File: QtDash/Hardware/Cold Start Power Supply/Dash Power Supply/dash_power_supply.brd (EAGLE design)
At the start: 160 x 100 mm, 26 parts, among them IC1 LM5060, Q1 IPB042N10N3GATMA1, Q2 IPB042N10N3GATMA1, Q3 600mA/40V

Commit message: bugfix/hardware-revA-issues: 	- added lm3488 5V SEPIC DC/DC converter -- components selected and first draft of layout 	- TODO: select components for input protection and layout the input proectection 	- TODO: add second 5V DC/DC
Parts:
- added C10, C11: 100u, dash_power_supply:C1210
- added C12: 4.7u, digital_dash:0603
- added C13: .68u, digital_dash:0603
- added C14, C15: 1n, digital_dash:0603
- added C6: 100n, digital_dash:0603
- added C7, C8, C9: 3.3u, dash_power_supply:PANASONIC_C
- added D10, D11: 3A/10V/280mV, SparkFun-DiscreteSemi:SOD-323
- added D9: STPS8H100G-TR, dash_power_supply:TO263
- added IC2: LM3488, dash_power_supply:VSSOP-8
- added L1: DRQ127-4R7-R, dash_power_supply:DRQ127
- added Q4: BSC027N04LSG, dash_power_supply:TDSON
- added R10: 20k, SparkFun-Resistors:0603
- added R11: 100R, digital_dash:0603
- added R12: 30.9k 1%, dash_power_supply:R1206
- added R13: 10k 1%, digital_dash:0603
- added R14: 75k, SparkFun-Resistors:0603
- added R15: 6mOhm, dash_power_supply:3216
- added R16: 270 1%, digital_dash:0603
- added R17: 0, SparkFun-Resistors:0603
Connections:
- removed net VOUT: D2.C, D3.C, Q2.3, R9.2
- new net 5V: C10.1, C11.1, D11.A, D9.3, R12.2
- new net N$11: Q4.4, R17.2
- new net N$12: C6.1, IC2.8, R10.1
- new net N$13: IC2.3, R12.1, R13.2
- new net N$15: IC2.6, R17.1
- new net N$16: C15.1, IC2.1, R11.1
- new net N$17: Q4.1, Q4.2, Q4.3, R11.2, R15.2
- new net N$18: C12.1, L1.3, Q4.5
- new net N$19: C12.2, D9.2, L1.4
- new net N$20: C14.1, IC2.2, R16.2
- new net N$21: C13.1, R16.1
- new net N$22: IC2.7, R14.2
- new net N$23: D10.C, R5.1
- new net VBATT: C7.+, C8.+, C9.+, D2.C, D3.C, L1.1, Q2.3, R10.2, R9.2
- net GND: now also C10.2, C11.2, C13.2, C14.2, C15.2, C6.2, C7.-, C8.-, C9.-, IC2.4, IC2.5, L1.2, R13.1, R14.1, R15.1
- net VIN_LM5060: now also D10.A, D11.C; no longer R5.1
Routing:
- net VBATT: track 0.00 -> 45.4 mm, vias 0 -> 2
- net N$17: track 0.00 -> 29.2 mm, vias 0 -> 2
- net N$13: track 0.00 -> 11.1 mm
- net N$16: track 0.00 -> 8.13 mm
- net N$12: track 0.00 -> 7.01 mm
- net N$20: track 0.00 -> 6.23 mm
- net N$22: track 0.00 -> 3.69 mm
- net N$15: track 0.00 -> 3.69 mm
- net N$11: track 0.00 -> 3.56 mm
- net N$21: track 0.00 -> 3.24 mm
- added copper zone on layer 1, net 5V
- added copper zone on layer 1, net GND
- added copper zone on layer 1, net N$14
- added copper zone on layer 1, net N$17
- added copper zone on layer 1, net N$18
- added copper zone on layer 1, net N$19
- added copper zone on layer 1, net VBATT

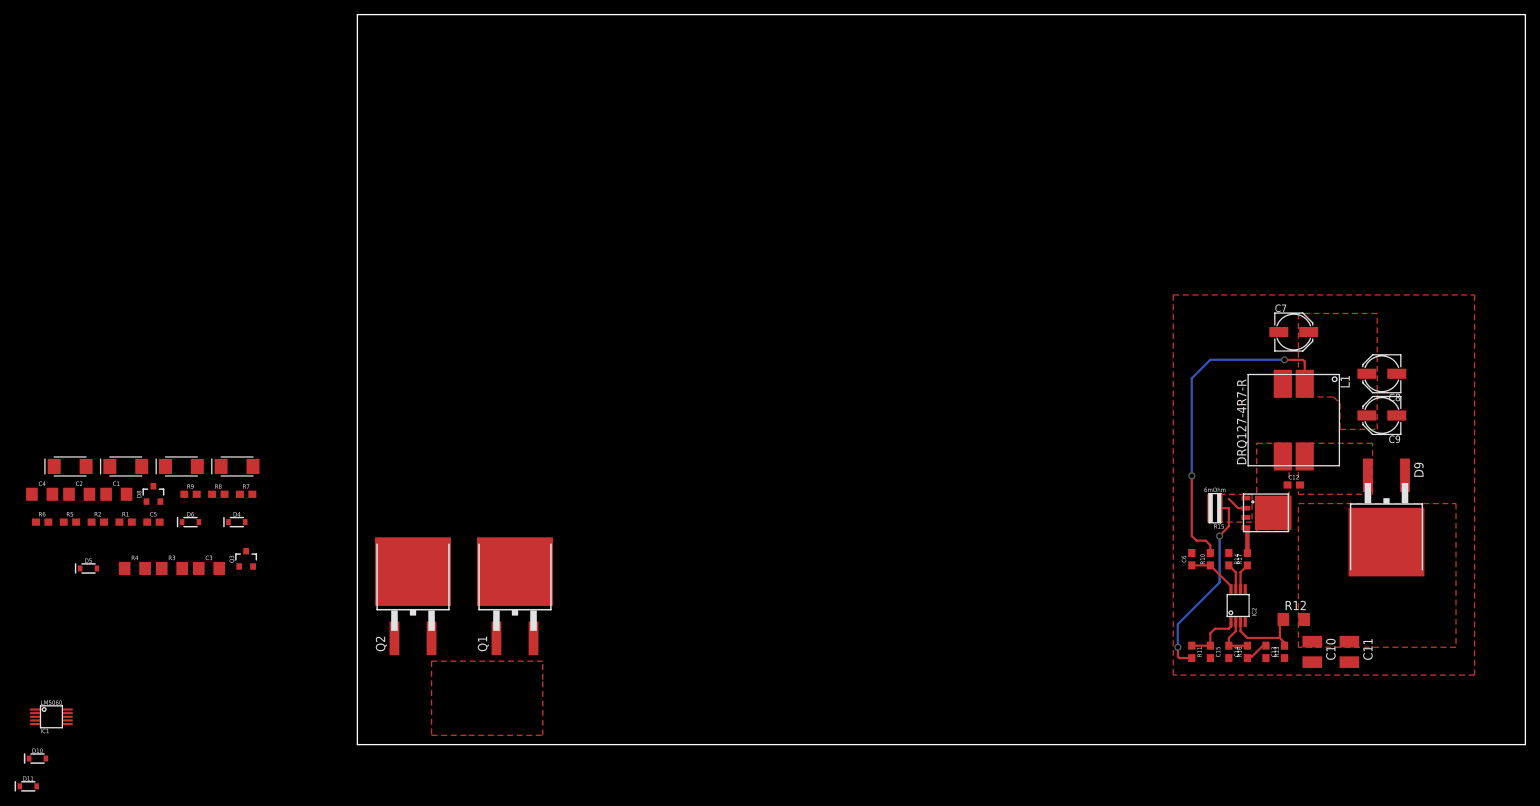
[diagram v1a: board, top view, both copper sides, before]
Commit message: bugfix/hardware-revA-issues: 	- first draft of cold start power supply board layout -- passed DRC
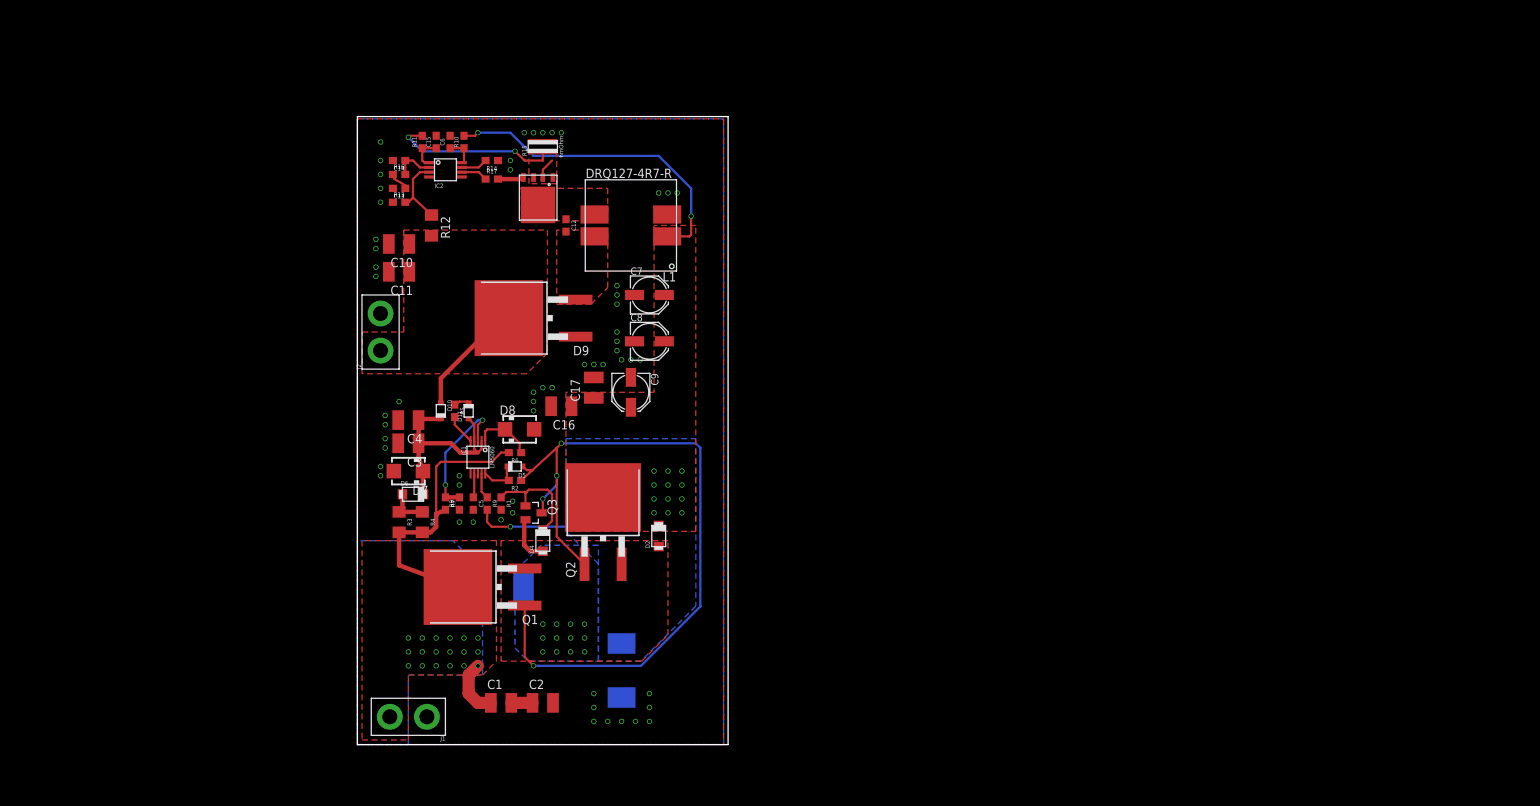
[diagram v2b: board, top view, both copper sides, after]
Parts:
- added C16: 4.7u, dash_power_supply:C1210
- added C17: 0.1u, dash_power_supply:C1210
- added J1, J2: (no value), SparkFun-Connectors:1X02_XTRA_BIG
- C1, C2, C4: value (none) -> 0.1u; device SparkFun-Capacitors:1206 -> dash_power_supply:C1210
- C3: value 4.7uF -> 4.7u; device SparkFun-Capacitors:1206 -> dash_power_supply:C1210
- C5: value 0.1uF -> 100n; device SparkFun-Capacitors:0603 -> digital_dash:0603
- D1, D3: device SparkFun-DiscreteSemi:DO-214AC -> dash_power_supply:SMC
- D10, D11, D5: value 3A/10V/280mV -> NSR0170HT1G; device SparkFun-DiscreteSemi:SOD-323 -> dash_power_supply:SOD-323
- D2: device SparkFun-DiscreteSemi:DO-214AC -> dash_power_supply:D0-219AB
- D4, D6: value 250mA/100V -> 200V; device SparkFun-DiscreteSemi:SOD-323 -> dash_power_supply:D0-219AB
- D7: value SMAJ36A -> 24V; device SparkFun-DiscreteSemi:DO-214AC -> dash_power_supply:SMA
- D8: value 68V -> 24V; device SparkFun-DiscreteSemi:SOT23-3 -> dash_power_supply:SMA
- Q3: value 600mA/40V -> BC816-25HVL; device SparkFun-DiscreteSemi:SOT23-3 -> dash_power_supply:SOT23
- moved C11 140.2 mm to (5.71, 64.8), turned to 180 degrees
- moved C10 137.0 mm to (5.71, 68.6), turned to 180 degrees
- moved R13 136.0 mm to (5.71, 74.3), turned to 0 degrees
- moved C13 134.7 mm to (5.71, 76.2), turned to 180 degrees
- moved R16 133.3 mm to (5.71, 78.1), turned to 0 degrees
- moved C14 132.1 mm to (5.71, 80.0), turned to 180 degrees
- moved R12 129.9 mm to (10.2, 71.1), turned to 270 degrees
- moved C15 127.0 mm to (10.8, 82.5), turned to 90 degrees
- moved R11 126.5 mm to (8.89, 82.5), turned to 90 degrees
- moved IC2 123.9 mm to (12.1, 78.7), turned to 0 degrees
- moved D9 120.0 mm to (24.1, 58.4), turned to 90 degrees
- moved R10 117.1 mm to (14.6, 82.5)
- moved C6 116.6 mm to (12.7, 82.5)
- moved R17 115.9 mm to (18.4, 77.5), turned to 0 degrees
- moved R14 114.8 mm to (18.4, 80.0), turned to 180 degrees
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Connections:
- net N$1 renamed G
- net N$5 renamed VIN_INTERNAL
- net 5V: now also D10.A, J2.1; no longer D11.A
- net GND: now also C16.2, C17.2, D8.A, J1.1, J2.2; no longer D8.1
- net N$23: now also D11.C; no longer D10.C
- net N$6: now also D8.C; no longer D8.3
- net VBATT: now also C16.1, C17.1
- net VIN: now also J1.2
- net VIN_LM5060: now also D10.C, D11.A; no longer D10.A, D11.C
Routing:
- net G: track 0.00 -> 108.8 mm, vias 0 -> 4
- net VIN: track 0.00 -> 46.8 mm, vias 0 -> 18
- net VIN_LM5060: track 0.00 -> 29.1 mm
- net VBATT: track 45.4 -> 63.8 mm, vias 2 -> 15
- net N$8: track 0.00 -> 18.1 mm, vias 0 -> 2
- net 5V: track 0.00 -> 16.9 mm
- net N$7: track 0.00 -> 15.1 mm
- net N$6: track 0.00 -> 8.31 mm
- net VIN_INTERNAL: track 0.00 -> 6.44 mm, vias 0 -> 12
- net N$4: track 0.00 -> 5.77 mm
- net GATE: track 0.00 -> 5.65 mm
- net N$3: track 0.00 -> 4.20 mm
- net N$10: track 0.00 -> 3.62 mm
- net N$17: track 29.2 -> 25.8 mm
- net N$16: track 8.13 -> 4.69 mm
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- added copper zone on layer 16, net GND
- added copper zone on layer 16, net VBATT
- added copper zone on layer 1, net VIN
- added copper zone on layer 16, net VIN
- added copper zone on layer 1, net VIN_INTERNAL
- added copper zone on layer 16, net VIN_INTERNAL
- removed copper zone on layer 1, net N$14
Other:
- board size 160 x 100 mm -> 50.8 x 86 mm

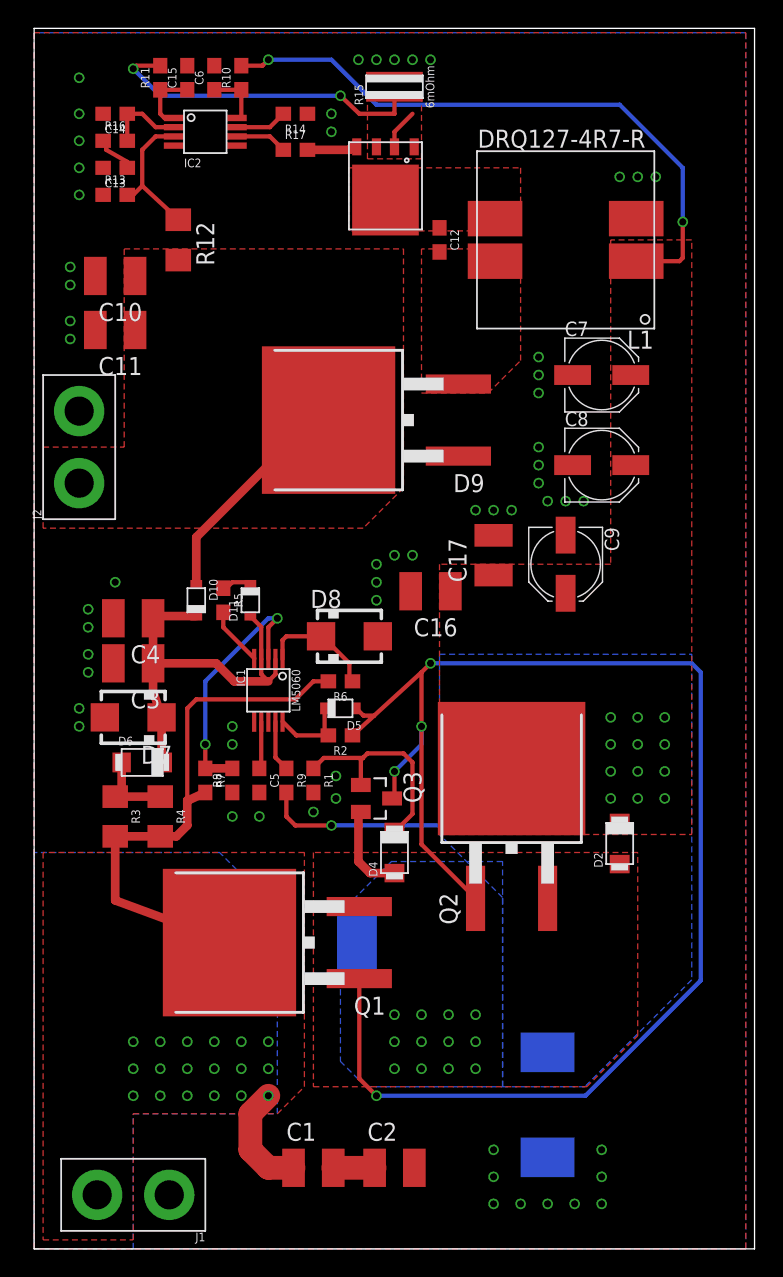
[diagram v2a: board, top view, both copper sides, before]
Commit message: bugfix/hardware-revA-issues: 	- added supply only board for testing separately and more cheaply 	- added resistor values to cold start board library
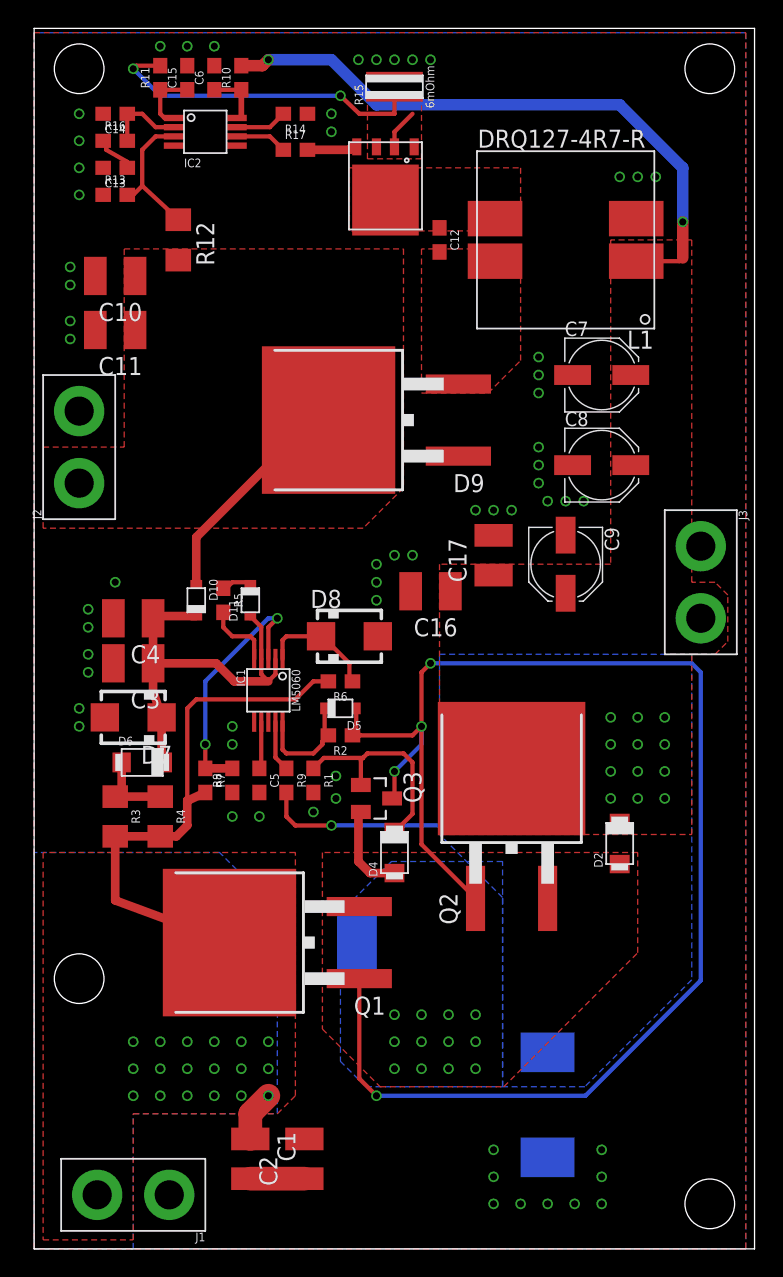
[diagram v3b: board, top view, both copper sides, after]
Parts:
- added J3: (no value), SparkFun-Connectors:1X02_XTRA_BIG
- moved C2 6.38 mm to (19.1, 6.35), turned to 90 degrees
- moved C1 4.49 mm to (15.2, 6.35), turned to 270 degrees
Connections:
- net GND: now also J3.1
- net VBATT: now also J3.2
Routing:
- net VIN: track 46.8 -> 42.5 mm
- net GATE: track 5.65 -> 7.98 mm
- net G: track 108.8 -> 107.3 mm
- net N$2: track 2.91 -> 3.81 mm
- net N$3: track 4.20 -> 4.94 mm

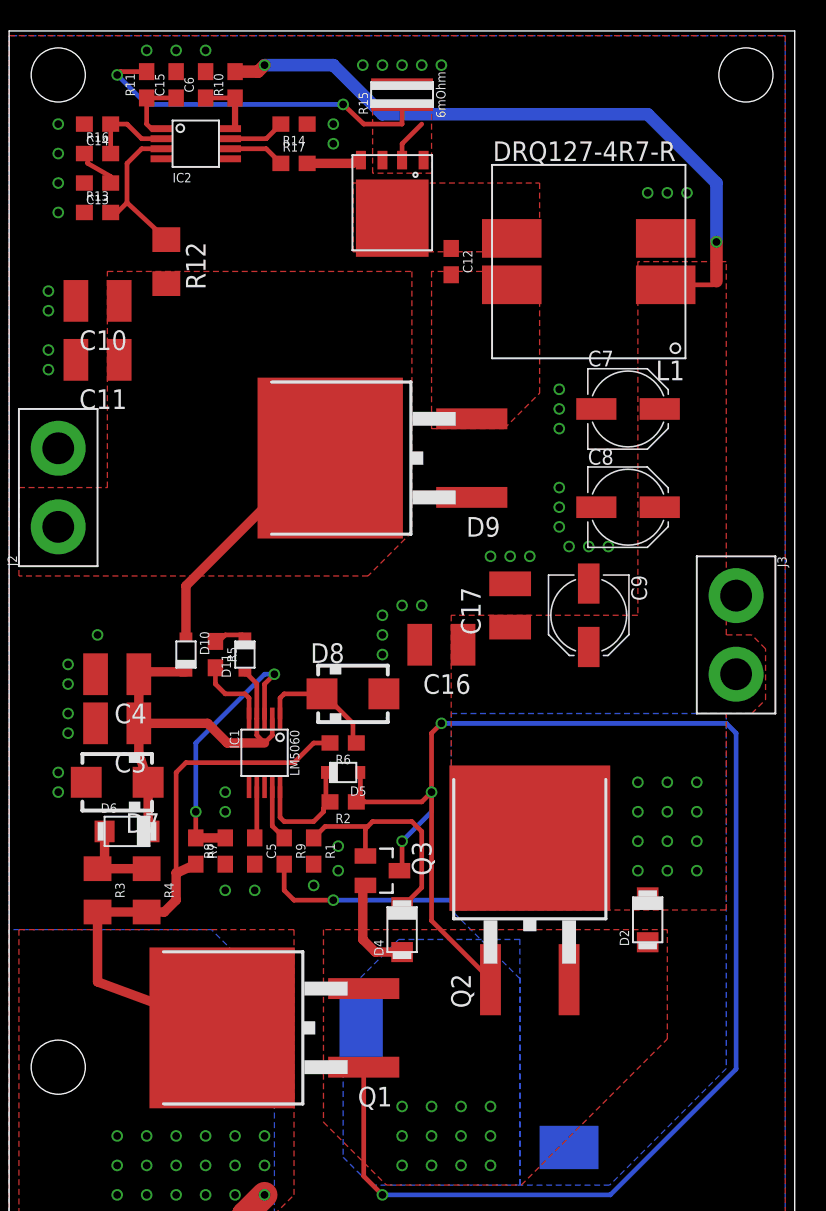
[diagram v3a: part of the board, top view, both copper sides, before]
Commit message: topic/component-optimization: 	- udpated supply and input protection board
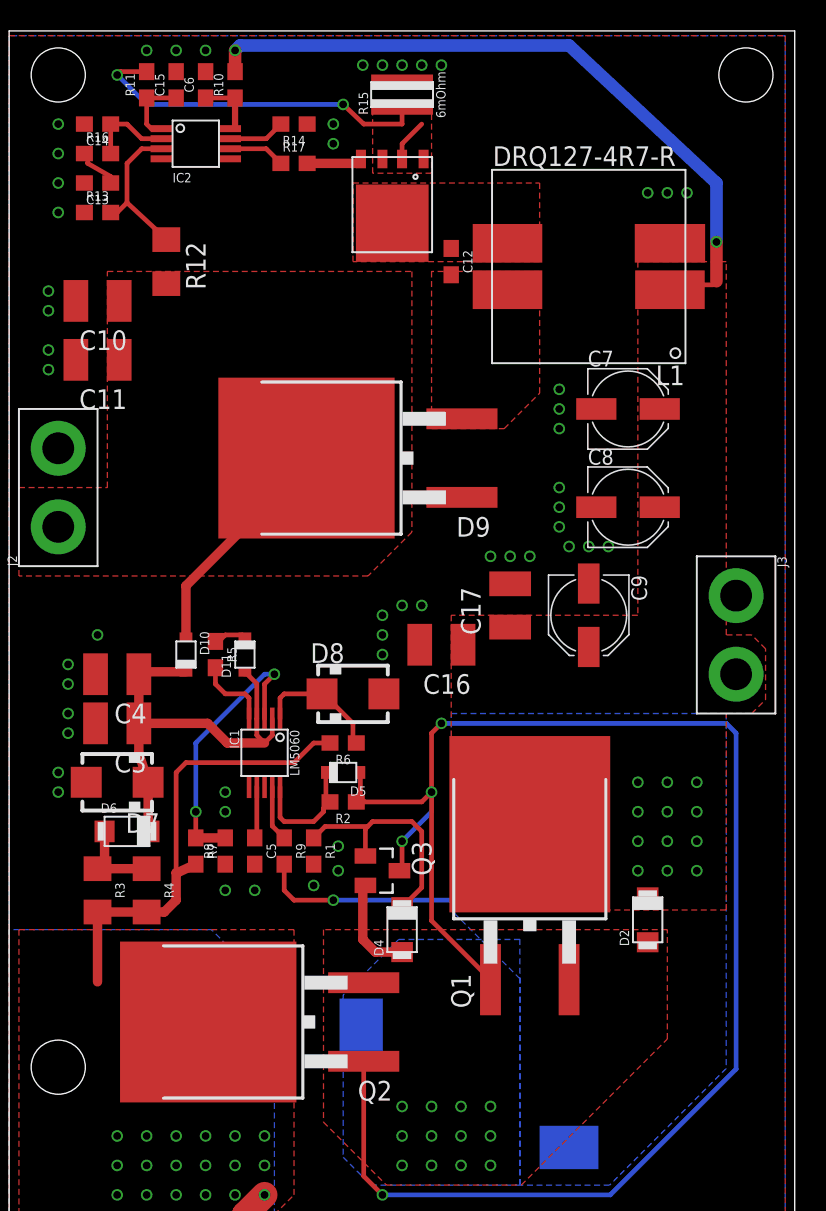
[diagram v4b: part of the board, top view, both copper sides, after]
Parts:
- R10: value 20k -> 20R; device SparkFun-Resistors:0603 -> digital_dash:0603
- moved Q1 18.8 mm to (33.7, 30.5), turned to 0 degrees
- moved Q2 18.6 mm to (17.1, 22.0), turned to 90 degrees
- moved D9 0.63 mm to (23.5, 58.4)
- moved L1 0.32 mm to (37.5, 70.8)
- moved Q4 0.13 mm to (24.8, 74.8)
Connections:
- net VBATT: now also Q1.3; no longer Q2.3
- net VIN: now also Q2.3; no longer Q1.3
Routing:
- net VIN: track 42.5 -> 33.9 mm
- net 5V: track 16.9 -> 15.0 mm
- net VBATT: track 63.8 -> 65.5 mm
